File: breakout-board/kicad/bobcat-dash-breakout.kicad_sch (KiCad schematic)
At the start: 143 parts, among them J1 TO PI (40-pin ribbon), J10 ADS1115, J11 LIGHTS, J12 COIL, J2 POWER IN, J3 TO 5V BUCK, J4 SWITCHES, J5 TACH, J6 FUEL, J7 HORN, J8 SILENCE, J9 MAX98357A, Q1 IRLZ44N, Q2 IRF4905, Q3 BC547B, Q4 BC547B, U1 PC817, U10 PC817, U4 PC817, U5 PC817, U6 CD4060BE, U7 PC817, U8 PC817, U9 PC817

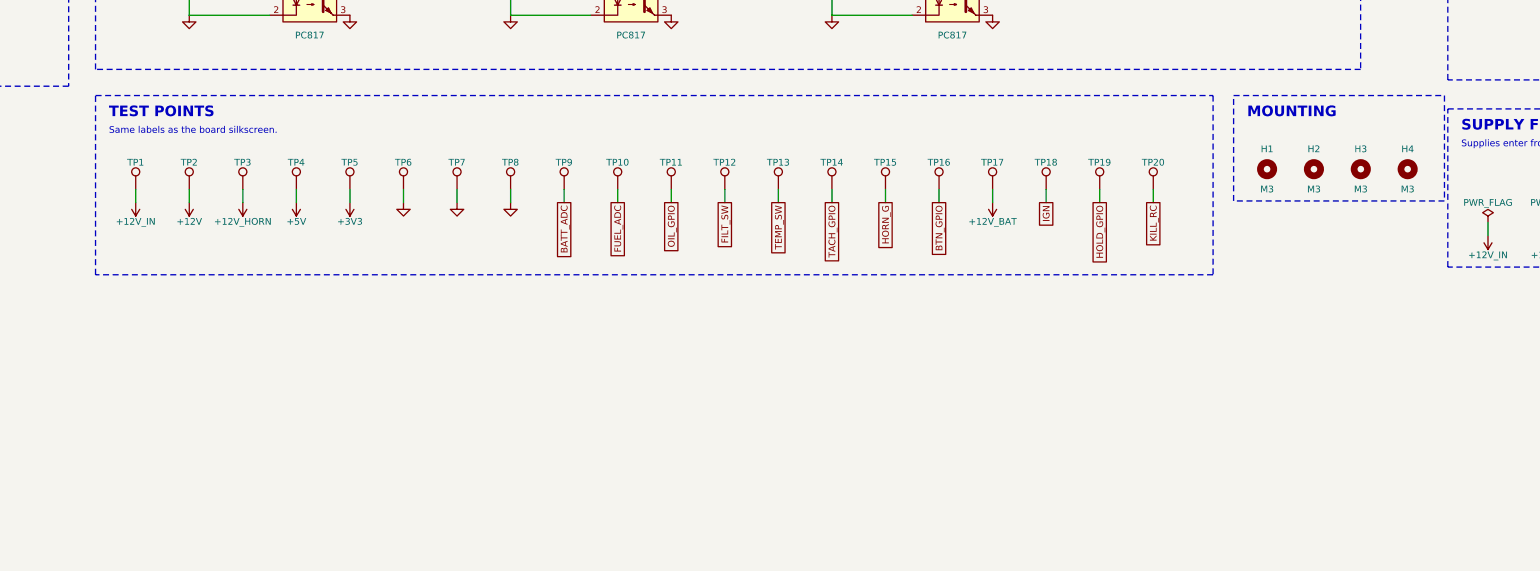
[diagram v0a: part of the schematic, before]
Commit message: Machine angle display, safe tilt zeroing, board rev 2.6 (latching TILT connector)
Software:
- Machine angle panel: roll (rear view) and pitch (side view) skid steer outlines that tilt with
  the machine, with amber/red limits (roll 8/15 deg, nose up 15/20, nose down 20/25; not Bobcat
  figures). Battery and fuel share one panel; warning tiles shorter. [tilt] enabled = false restores
  the original layout.
- tilt.py: LSM6DSOX reader with gyro/accelerometer blending (bumps move it < 1 deg), start-up
  averaging so a restart on a slope reads the true angle at once, and --zero-tilt that refuses on a
  slope (> 5 deg) or while moving unless --force.
- Simulator: Left/Right roll, , / . pitch, 0 level.
- Light indicators back to the small icons by default (display = "tiles" still available).

Breakout board:
- rev 2.5: TILT connector J13 (GND, 3V3, SDA, SCL) with 100R SDA/SCL and 47R 3V3 protection.
- rev 2.6: J13 is a latching Molex Micro-Fit 3.0 (43650-0415). Harness stays Phoenix MSTB
  (14-16 AWG); README covers securing the plugs against vibration.
- Schematic block subtitles now wrap to fit their boxes.

Docs and BOM updated (tilt sensor, Micro-Fit housing and pins, sensor cable).

Co-Authored-By: Claude Opus 5.5 <noreply@anthropic.com>
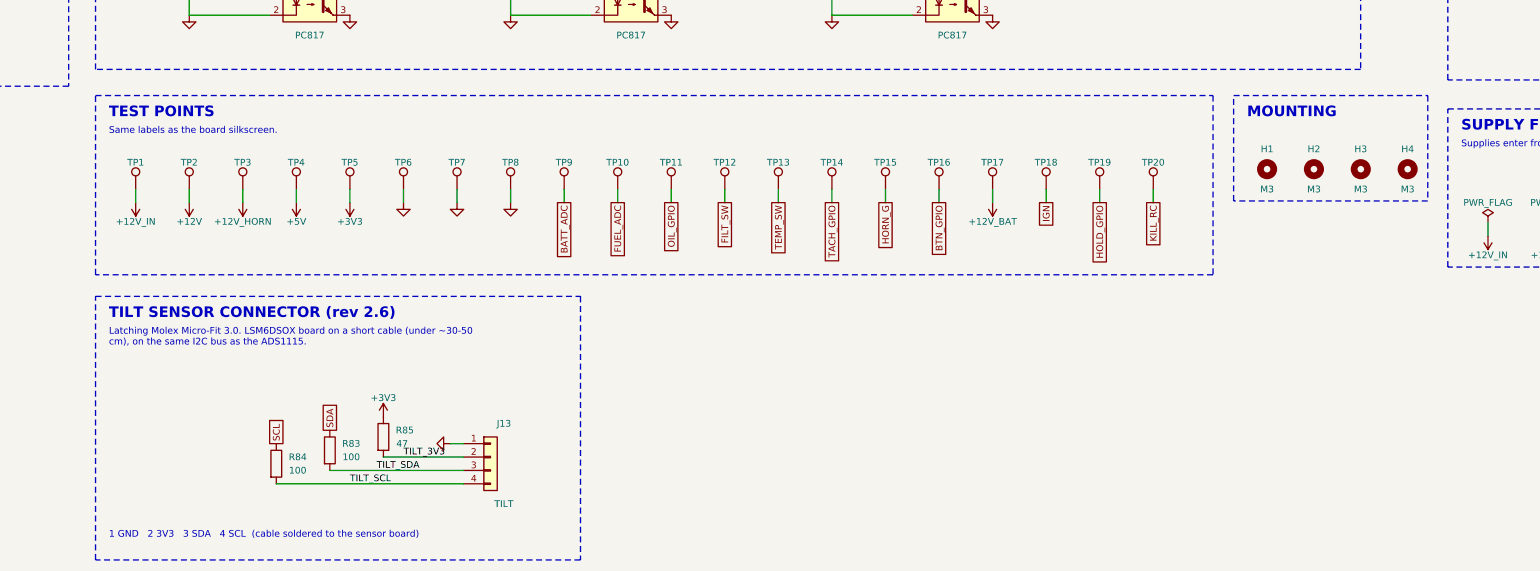
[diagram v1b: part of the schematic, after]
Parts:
- added J13: TILT, Connector_Molex:Molex_Micro-Fit_3.0_43650-0415_1x04_P3.00mm_Vertical, symbol Connector_Generic:Conn_01x04
- added R83, R84: 100, Resistor_THT:R_Axial_DIN0207_L6.3mm_D2.5mm_P7.62mm_Horizontal, symbol Device:R
- added R85: 47, Resistor_THT:R_Axial_DIN0207_L6.3mm_D2.5mm_P7.62mm_Horizontal, symbol Device:R
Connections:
- net +3V3: now also R85.1
- net GND: now also J13.1 (Pin_1)
- net SCL: now also R84.1
- net SDA: now also R83.1
- new net TILT_3V3: J13.2 (Pin_2), R85.2
- new net TILT_SCL: J13.4 (Pin_4), R84.2
- new net TILT_SDA: J13.3 (Pin_3), R83.2
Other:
- note added: "1 GND 2 3V3 3 SDA 4 SCL (cable soldered to the sensor board)"
- note added: "Latching Molex Micro-Fit 3.0. LSM6DSOX board on a short cable (under ~30-50 cm), on the same I2C bus as the ADS1115."
- note added: "TILT SENSOR CONNECTOR (rev 2.6)"

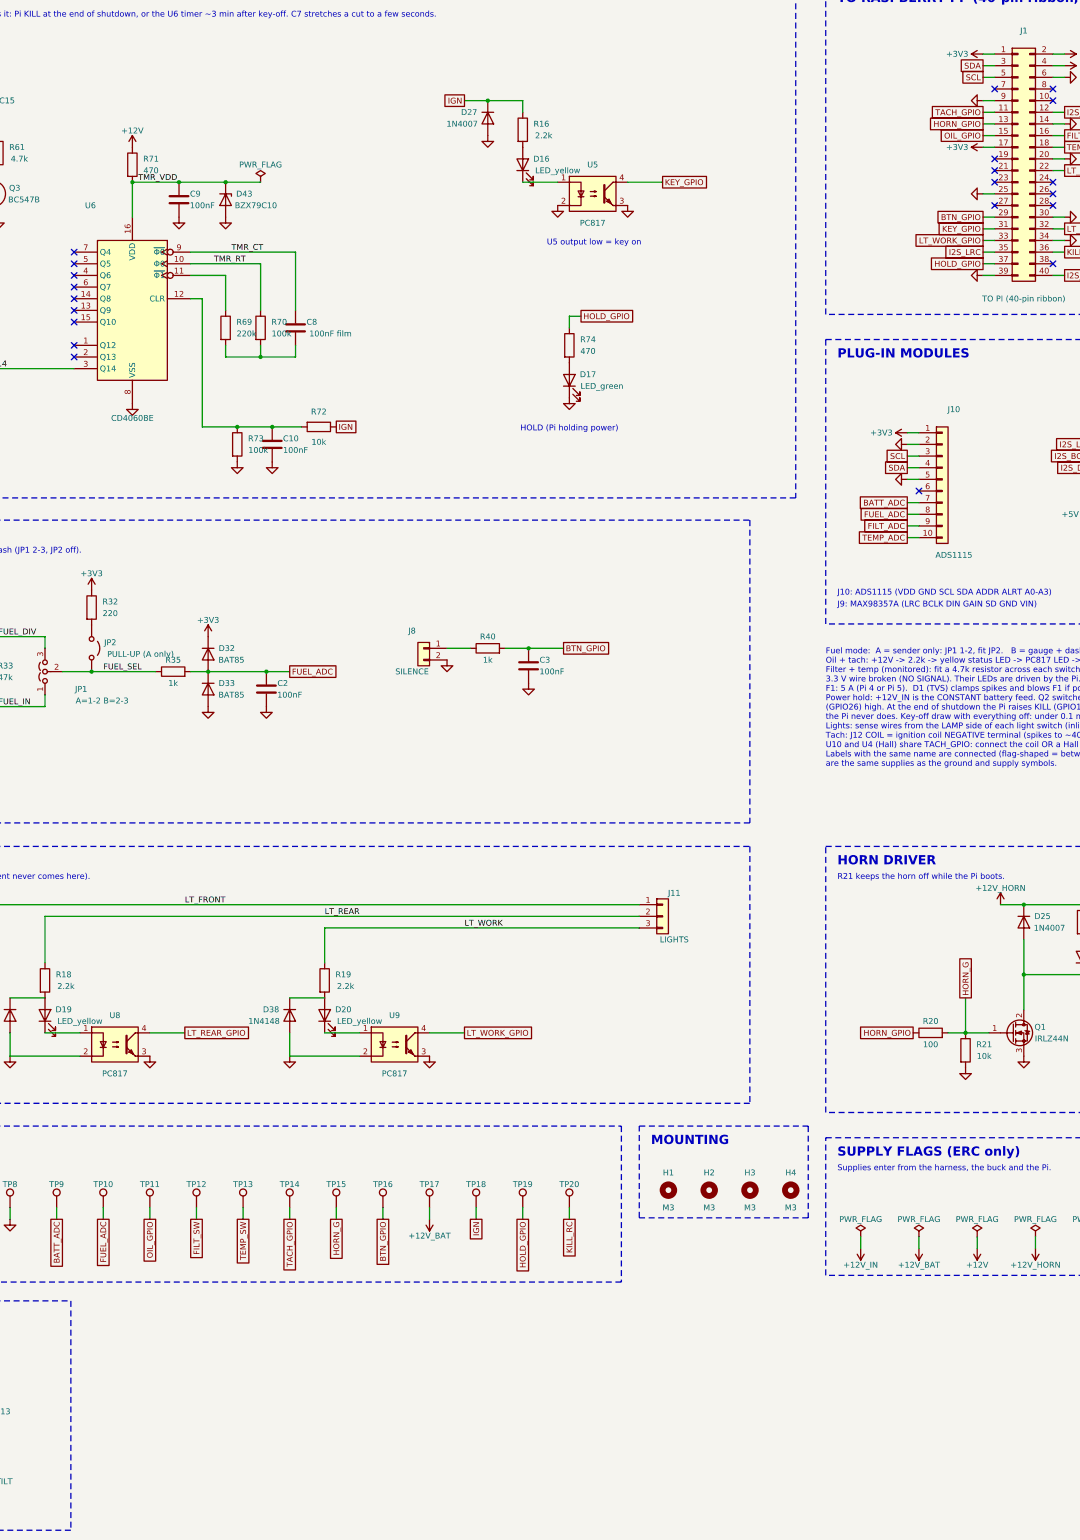
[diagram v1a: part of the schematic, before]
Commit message: Temperatures, tilt sensor fault handling, board rev 2.7, drilling template
- Board rev 2.7 (162 x 134 mm): on-board DS18B20 box-air sensor (U11) and a
  latching Micro-Fit 3-pin TEMP PROBE header (J14) on the 1-Wire bus (GPIO 4)
- Dash: BOX HOT warning (50/65 C, 2 C hysteresis) and ambient readout for
  cab/outside probes (each or averaged); --temps lists the sensors
- Tilt sensor fault handling: missing/dead/nonsense sensor shows "--" instead
  of a made-up angle, re-initialises on its own, logs once
- Simulator: '-' unplugs the tilt sensor, '=' steps the box temperature
- Printable 1:1 drilling template (breakout-board/docs/mounting-template.pdf)
  with check rulers and Actual-size print preference

Co-Authored-By: Claude Opus 5.5 <noreply@anthropic.com>
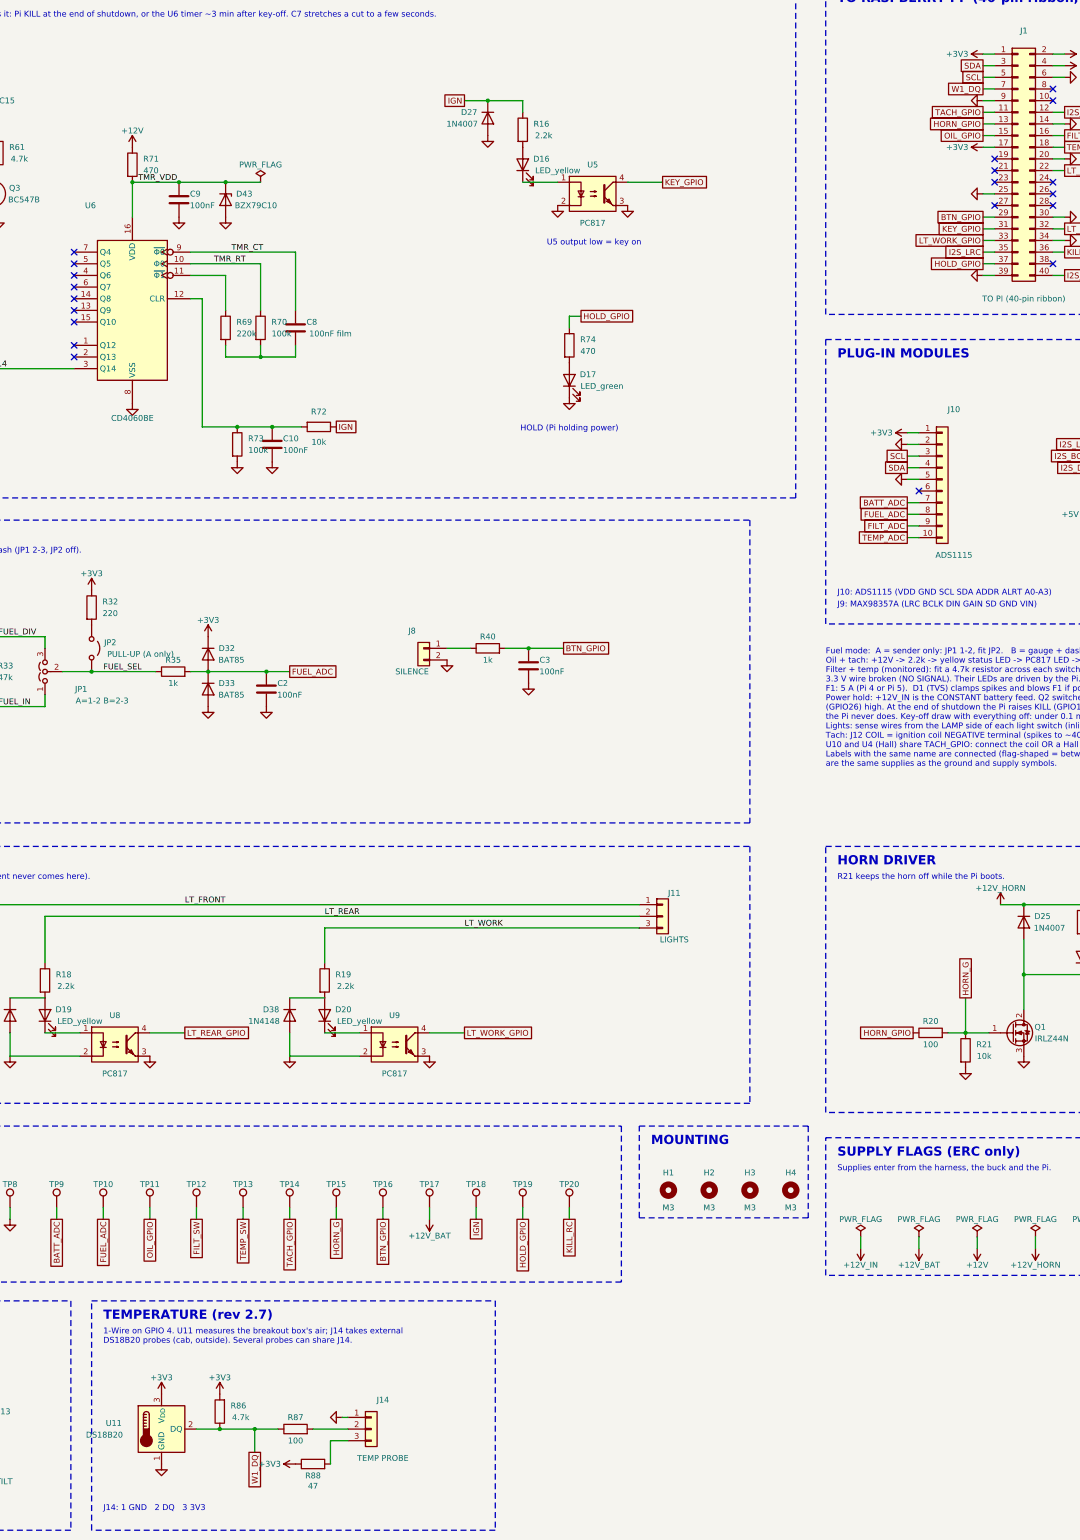
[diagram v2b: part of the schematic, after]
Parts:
- added J14: TEMP PROBE, Connector_Molex:Molex_Micro-Fit_3.0_43650-0315_1x03_P3.00mm_Vertical, symbol Connector_Generic:Conn_01x03
- added R86: 4.7k, Resistor_THT:R_Axial_DIN0207_L6.3mm_D2.5mm_P7.62mm_Horizontal, symbol Device:R
- added R87: 100, Resistor_THT:R_Axial_DIN0207_L6.3mm_D2.5mm_P7.62mm_Horizontal, symbol Device:R
- added R88: 47, Resistor_THT:R_Axial_DIN0207_L6.3mm_D2.5mm_P7.62mm_Horizontal, symbol Device:R
- added U11: DS18B20, Package_TO_SOT_THT:TO-92_Inline_Wide, symbol Sensor_Temperature:DS18B20
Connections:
- net +3V3: now also R86.2, R88.1, U11.3 (V_{DD})
- net GND: now also J14.1 (Pin_1), U11.1 (GND)
- net W1_DQ: now reaches J1.7 (Pin_7)
- net W1_DQ: now also R86.1, R87.1, U11.2 (DQ)
- new net: J14.2 (Pin_2), R87.2
- new net: J14.3 (Pin_3), R88.2
- no-connect marks 23 -> 22
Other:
- note added: "1-Wire on GPIO 4. U11 measures the breakout box's air; J14 takes external DS18B20 probes (cab, outside). Several probes can share J14."
- note added: "J14: 1 GND 2 DQ 3 3V3"
- note added: "TEMPERATURE (rev 2.7)"
